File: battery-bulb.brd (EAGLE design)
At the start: 21.6 x 20.3 mm, 12 parts, among them J1 USB-MICROB, U1 MCP73831, U2 RT9013-XXXB

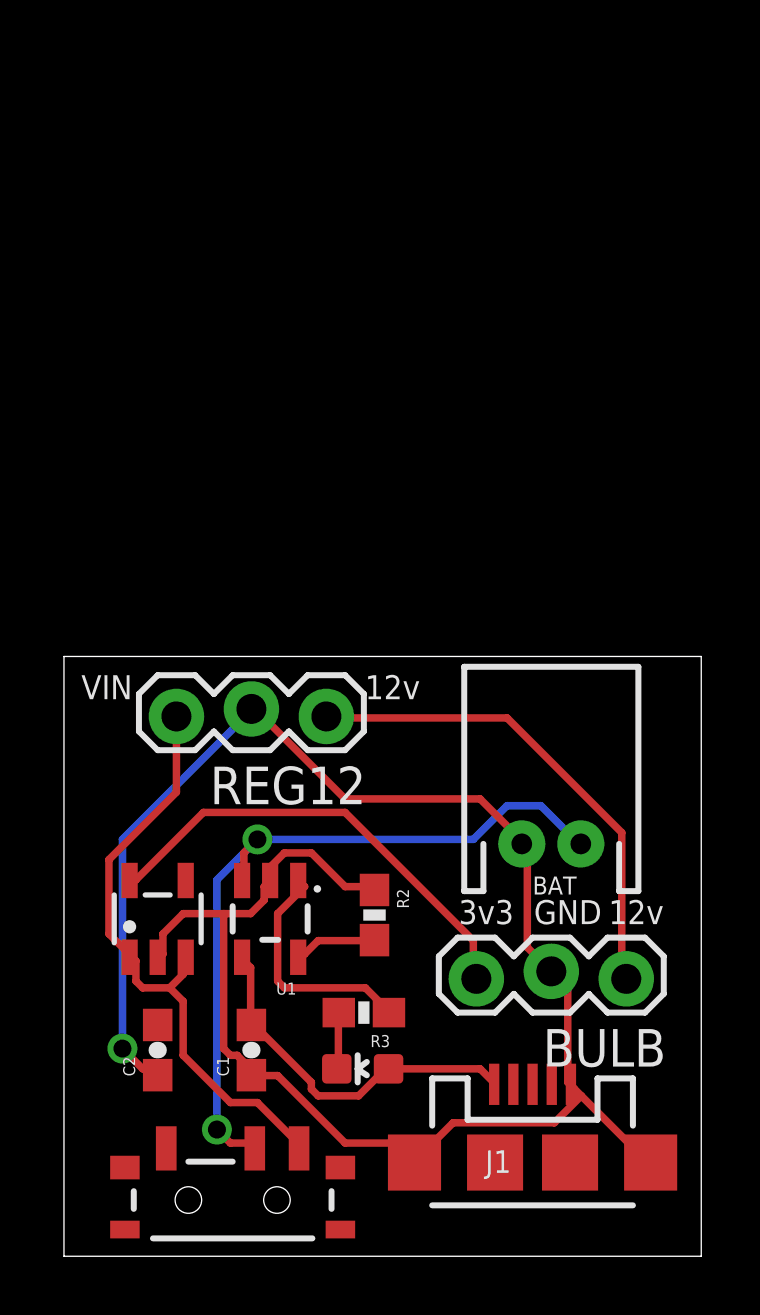
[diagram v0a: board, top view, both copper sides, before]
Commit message: board revision 2
extend the board with direct connection to the bulb's logic board
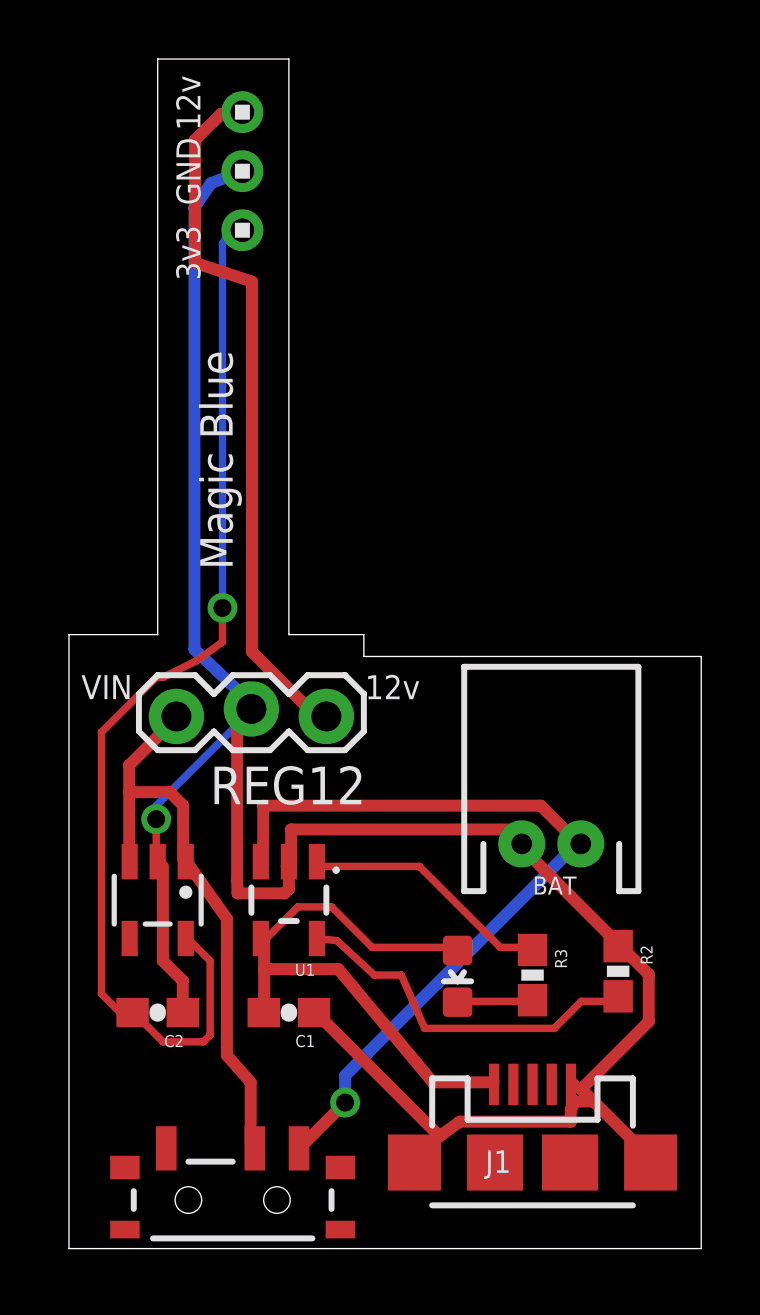
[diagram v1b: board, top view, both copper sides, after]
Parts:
- BULB: value (none) -> 1X3; device SparkFun-Connectors:1X03_LOCK -> headers(2mm):1X3
- moved BULB 30.2 mm to (36.5, 64.7), turned to 90 degrees
- moved R2 8.47 mm to (49.3, 37.6)
- moved R3 5.85 mm to (46.4, 37.5), turned to 270 degrees
- moved D3 4.49 mm to (43.8, 37.4), turned to 180 degrees
- moved C1 1.80 mm to (38.1, 36.2), turned to 180 degrees
- moved C2 1.27 mm to (33.7, 36.2), turned to 180 degrees
- moved U1 0.90 mm to (38.1, 40.0)
- moved U2 0.64 mm to (33.7, 40.0), turned to 180 degrees
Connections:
- net 12V: now also BULB.3; no longer BULB.1
- net VBAT: now also S1.1; no longer S1.2
- net VDD: now also BULB.1, C2.2; no longer BULB.3
- net VIN: now also S1.2; no longer S1.1
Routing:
- net VDD: track 15.7 -> 36.5 mm, vias 0 -> 1
- net GND: track 68.4 -> 81.6 mm
- net N$1: track 2.80 -> 12.3 mm
- net VBUS: track 12.4 -> 20.0 mm
- net 12V: track 16.6 -> 24.2 mm
- net VBAT: track 25.5 -> 27.5 mm, vias 2 -> 1
- net N$5: track 1.96 -> 2.55 mm
- net VIN: track 20.6 -> 20.1 mm
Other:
- board size 21.6 x 20.3 mm -> 21.4 x 40.3 mm
- board text added: "Magic Blue"
- board text added: "https://github.com/urish/battery-bulb"
